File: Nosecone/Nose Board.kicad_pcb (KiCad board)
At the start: 2 copper layers, 45.7 x 63.5 mm, 55 parts, among them J1 Conn_01x02, J2 Conn_02x04_Odd_Even, J3 Conn_02x03_Odd_Even, J4 Conn_Coaxial, J5 Conn_01x02, Q1 Q_PMOS_DGS, Q2 Q_PMOS_DGS, U1 RS485_converter_ISL83488, U10 MS5803-14BA, U11 MS5803-14BA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

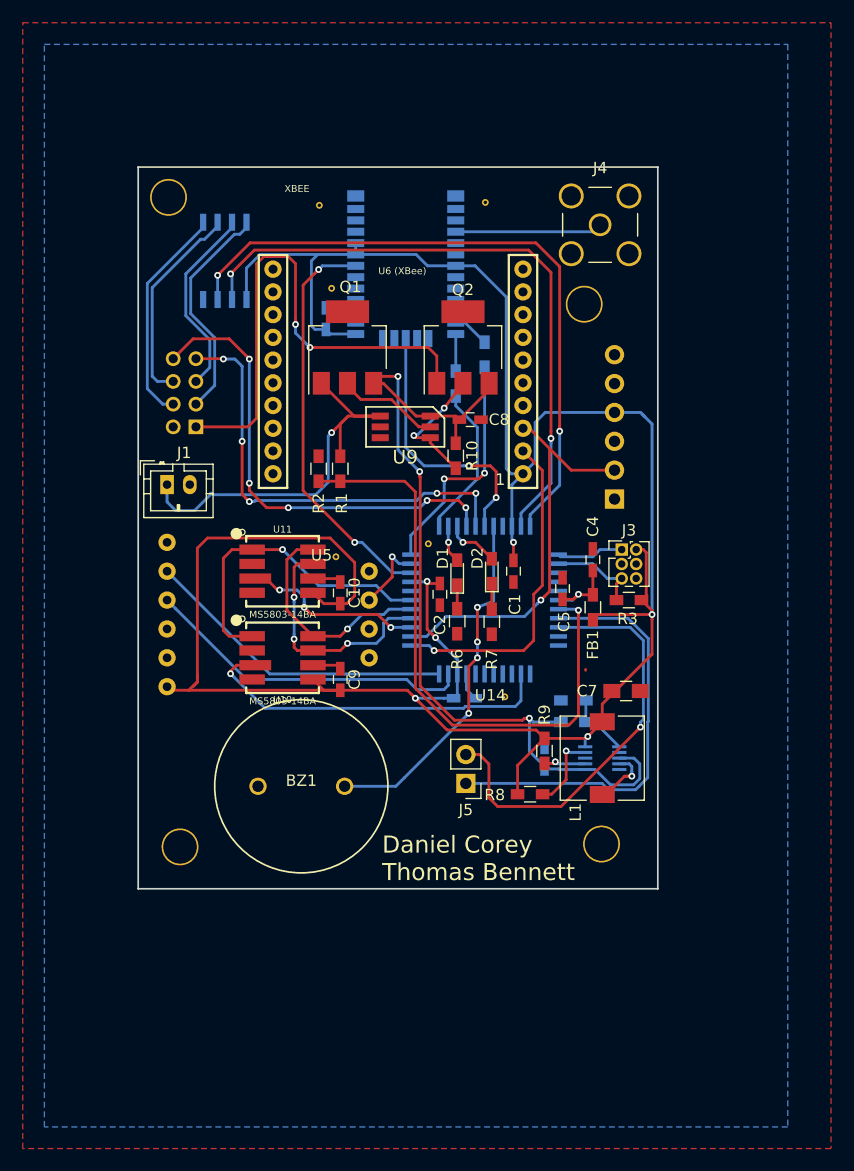
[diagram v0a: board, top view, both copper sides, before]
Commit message: Fixed via and board outline issues
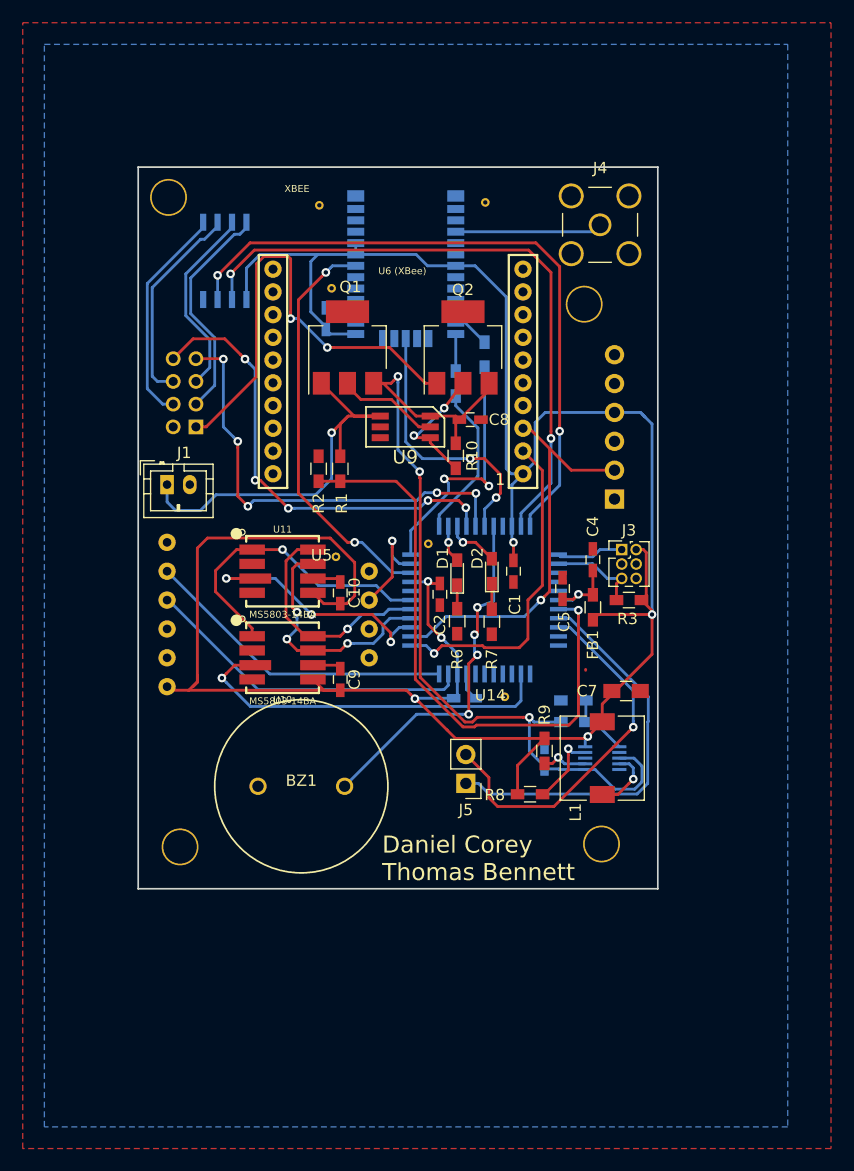
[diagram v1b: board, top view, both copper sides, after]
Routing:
- net /P1_CS: track 16.0 -> 22.4 mm
- net /A2: track 37.6 -> 32.6 mm
- net VBUS: track 45.0 -> 40.9 mm
- net /IMU_INT: track 6.53 -> 9.32 mm
- net /A1: track 37.6 -> 35.2 mm
- net /GPS1_TXD: track 21.0 -> 23.0 mm
- net +BATT: track 36.8 -> 38.4 mm
- net /P2_CS: track 32.1 -> 33.3 mm
- net /Debug_RX: track 41.6 -> 40.6 mm
- net /P_SCLK: track 27.7 -> 26.9 mm
- net /Vbatt_meas: track 53.3 -> 52.5 mm
- net /P_MOSI: track 21.1 -> 21.7 mm
- net VDC: track 77.3 -> 77.9 mm
- net +3V3: track 225.3 -> 224.7 mm
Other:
- net class Default: via_dia 0.6 -> 0.762; via_drill 0.3 -> 0.381
- net class differential: via_dia 0.6 -> 0.762; via_drill 0.3 -> 0.381
- rule via_min_drill: 0.3 -> 0.381
- rule via_min_size: 0.4 -> 0.635
